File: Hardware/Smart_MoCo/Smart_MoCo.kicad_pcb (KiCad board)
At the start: 4 copper layers, 33.4 x 42.3 mm, 32 parts, among them J1 Conn_01x04, J2 1722861102, J4 1722861102, U1 STM32F042F6Px, U2 VNH5019A-E, U3 SN65HVD232, U4 AP62200WU

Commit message: Melt traces
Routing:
- net IN_A: track 18.2 -> 17.5 mm
- net LED_STATUS: track 21.8 -> 21.2 mm
- net LIM_B: track 19.7 -> 19.2 mm

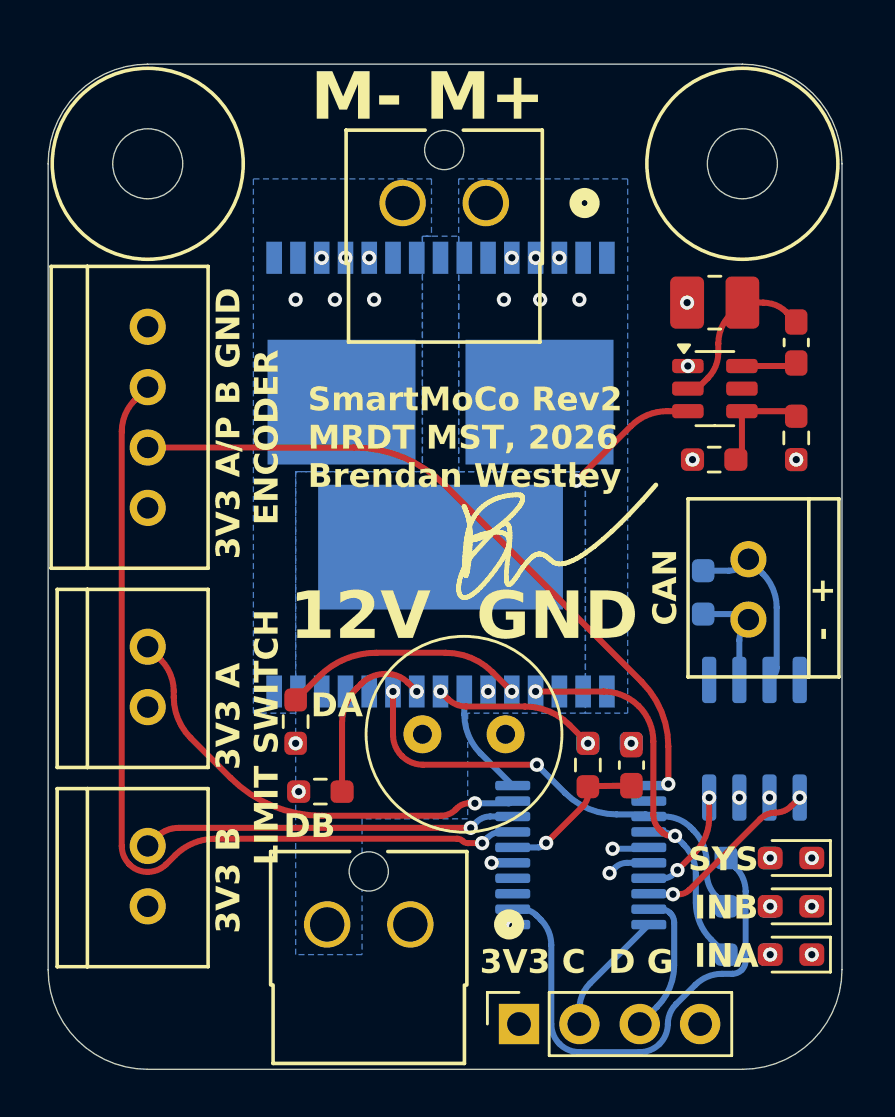
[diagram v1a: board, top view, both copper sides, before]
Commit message: Move mounting hole
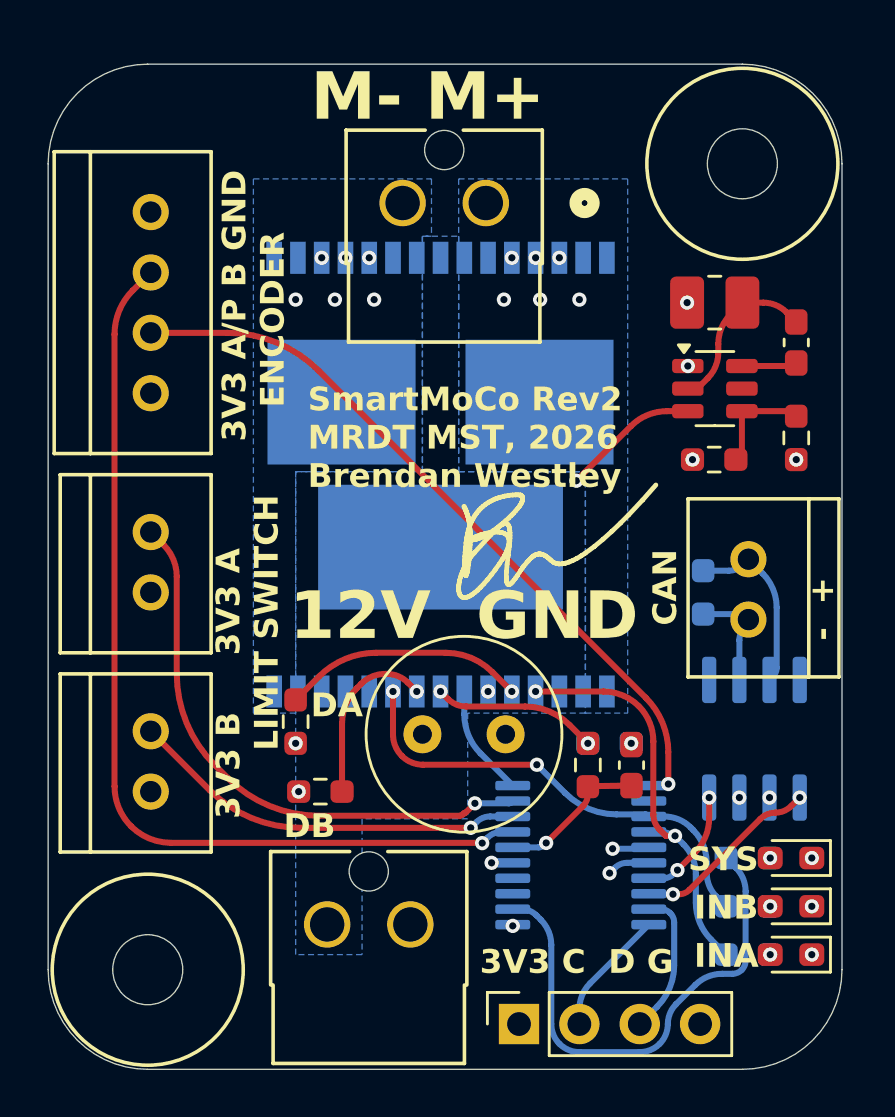
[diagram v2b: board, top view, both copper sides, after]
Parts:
- moved H2 33.9 mm to (140.1, 94.4)
- moved Conn3 4.83 mm to (140.2, 70.1)
- moved Conn4 4.83 mm to (140.2, 86.9)
- moved Conn5 4.83 mm to (140.2, 78.5)
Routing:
- net LIM_B: track 19.2 -> 24.0 mm
- net ENC_B: track 37.3 -> 40.4 mm
- net ENC_A/PWM: track 30.0 -> 31.6 mm
- net LIM_A: track 15.8 -> 16.8 mm

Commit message: Change signal connectors to horizontal JST SH
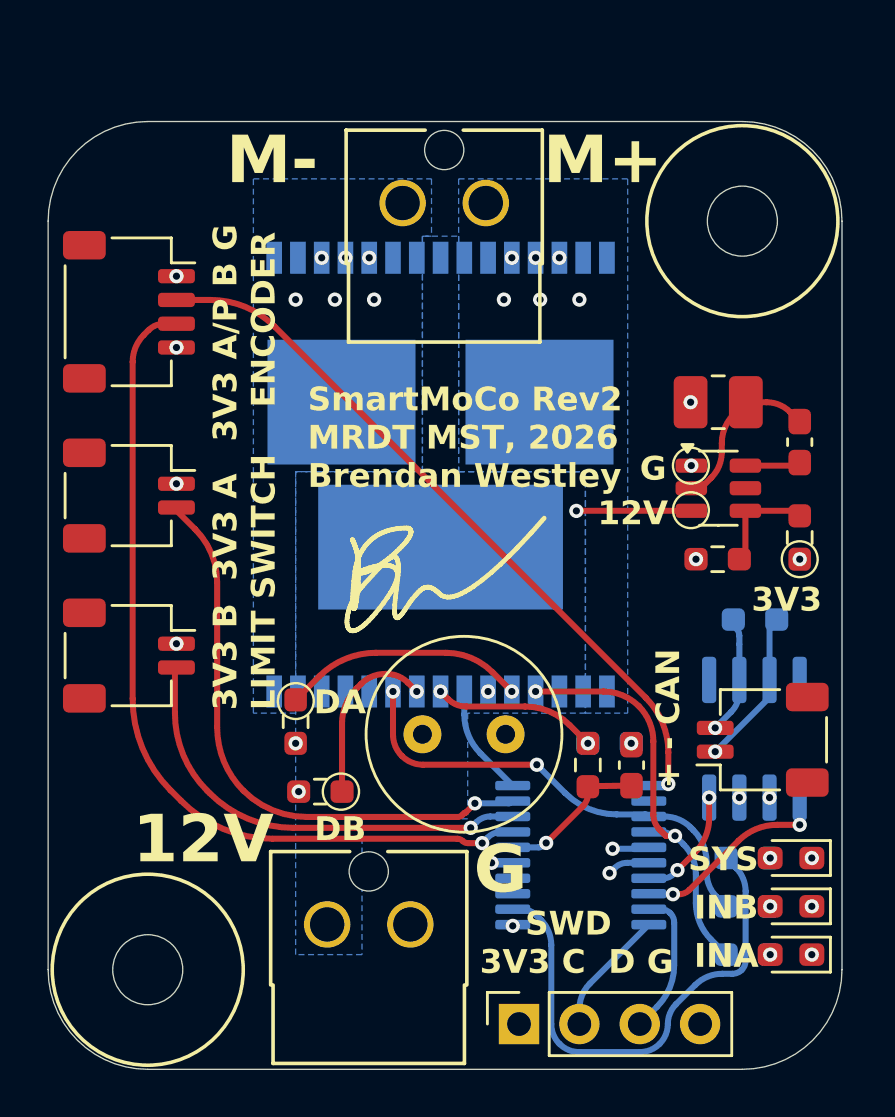
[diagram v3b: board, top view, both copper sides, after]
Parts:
- removed Conn1, Conn4, Conn5: Molex_SL_02, MRDT_Connectors:MOLEX_SL_02_Vertical
- removed Conn3: Molex_SL_04, MRDT_Connectors:MOLEX_SL_04_Vertical
- added J3: Conn_01x02, Connector_JST:JST_SH_SM02B-SRSS-TB_1x02-1MP_P1.00mm_Horizontal, F.Cu at (166.0, 84.7)
- added J5: Conn_01x04, Connector_JST:JST_SH_SM04B-SRSS-TB_1x04-1MP_P1.00mm_Horizontal, F.Cu at (139.3, 66.7)
- added J6: Conn_01x02, Connector_JST:JST_SH_SM02B-SRSS-TB_1x02-1MP_P1.00mm_Horizontal, F.Cu at (139.3, 81.1)
- added J7: Conn_01x02, Connector_JST:JST_SH_SM02B-SRSS-TB_1x02-1MP_P1.00mm_Horizontal, F.Cu at (139.3, 74.4)
- moved G*** 6.33 mm to (165.2, 70.9)
- moved REF** 4.90 mm to (152.4, 77.7)
- moved L2 4.19 mm to (164.1, 70.5)
- moved R5 4.19 mm to (167.5, 76.2)
- moved R6 4.19 mm to (164.1, 77.1)
- moved U4 4.19 mm to (164.1, 74.1)
- moved C10 4.19 mm to (167.5, 72.2)
- moved R9 2.46 mm to (165.6, 79.6), turned to 180 degrees
- moved H1 2.41 mm to (165.1, 62.9)
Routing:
- net ENC_B: track 40.4 -> 36.3 mm
- net LIM_A: track 16.8 -> 18.9 mm
- net CANH: track 7.48 -> 5.47 mm, vias 0 -> 1
- net +12V: track 5.80 -> 4.84 mm
- net LIM_B: track 24.0 -> 24.7 mm
- net CAN_TX: track 7.88 -> 8.53 mm
- net CANL: track 4.51 -> 4.75 mm, vias 0 -> 1
- net +3V3: vias 7 -> 10
- net GND: vias 16 -> 17
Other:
- board size 33.4 x 42.3 mm -> 33.4 x 39.9 mm
- board text added: "+ - CAN"
- board text added: "12V"
- board text added: "3V3"
- board text added: "3V3 A/P B G ENCODER"
- board text added: "G"
- board text added: "M+"
- board text added: "M-"
- board text added: "SWD 3V3 C D G"
- board text removed: "- +"
- board text removed: "12V GND"
- board text removed: "3V3 A/P B GND ENCODER"
- board text removed: "3V3 C D G"
- board text removed: "CAN"
- board text removed: "M- M+"

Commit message: Shrink board to 27x40mm
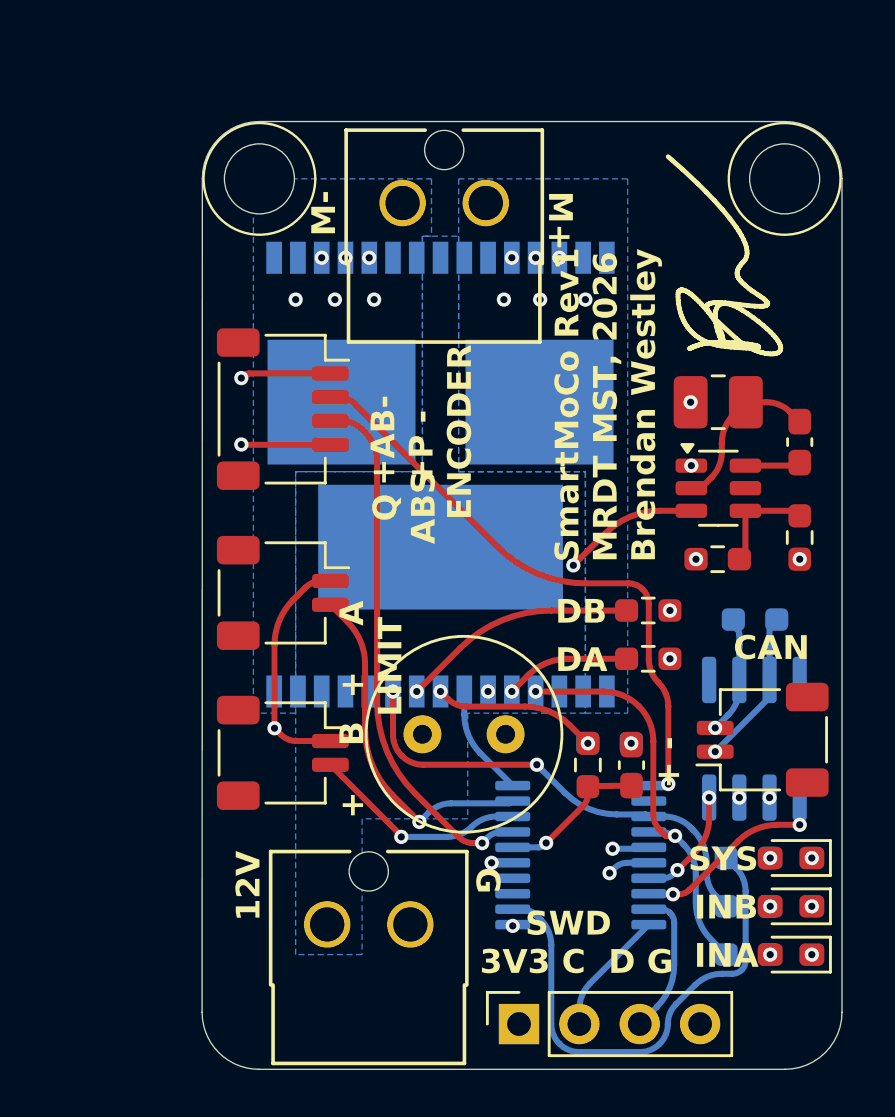
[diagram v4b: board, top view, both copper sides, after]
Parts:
- H1, H2: footprint MRDT_Drill_Holes:4_40_Hole -> Local Libraries:Minimal_4_40_Hole
- moved H2 33.6 mm to (144.8, 61.1)
- moved G*** 24.8 mm to (147.3, 88.0), turned to -90 degrees
- moved REF** 17.8 mm to (164.3, 64.5), turned to 90 degrees
- moved R3 15.8 mm to (161.1, 79.2), turned to 180 degrees
- moved R2 15.1 mm to (161.1, 81.3), turned to 0 degrees
- moved J5 7.66 mm to (145.8, 70.8)
- moved J6 7.66 mm to (145.8, 85.2)
- moved J7 7.66 mm to (145.8, 78.5)
- moved H1 2.51 mm to (166.9, 61.1)
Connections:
- R2 pad 1: +3V3 -> Net-(U2-EN/DIAGA)
- R2 pad 2: Net-(U2-EN/DIAGA) -> +3V3
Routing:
- net ENC_B: track 36.3 -> 22.4 mm
- net +3V3: track 2.68 -> 16.5 mm, vias 10 -> 9
- net LIM_B: track 24.7 -> 14.6 mm
- net LIM_A: track 18.9 -> 9.17 mm
- net ENC_A/PWM: track 31.3 -> 25.5 mm
- net Net-(U2-EN/DIAGA): track 10.3 -> 5.28 mm
- net GND: track 0.83 -> 4.58 mm
- net Net-(U2-EN/DIAGB): track 7.46 -> 9.98 mm
- net +12V: track 4.84 -> 5.76 mm
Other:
- board size 33.4 x 39.9 mm -> 26.9 x 39.9 mm
- board text added: "+ -"
- board text added: "+ B + A LIMIT"
- board text added: "+AB- +P - ENCODER"
- board text added: "CAN"
- board text added: "Q ABS"
- board text added: "SmartMoCo Rev1 MRDT MST, 2026 Brendan Westley"
- board text removed: "+ - CAN"
- board text removed: "3V3"
- board text removed: "3V3 A/P B G ENCODER"
- board text removed: "3V3 B 3V3 A LIMIT SWITCH"
- board text removed: "SmartMoCo Rev2 MRDT MST, 2026 Brendan Westley"

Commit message: Update gerbs and bom
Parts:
- renumbered C2 to C1, C7 to C2, C10 to C3, J3 to J1, J5 to J2, J6 to J3, J7 to J4, J1 to J5, J4 to J6, J2 to J7, L2 to L1, R4 to R1, R12 to R10, R8 to R4, R9 to R5, R5 to R6, R6 to R7, R10 to R8, R11 to R9
